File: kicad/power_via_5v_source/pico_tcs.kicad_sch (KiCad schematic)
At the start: 11 parts, among them J1 TCS/Power, J2 Conn_01x20_Male, J3 Conn_01x20_Male, J4 Keypad, J5 Display, U2 ULN2003

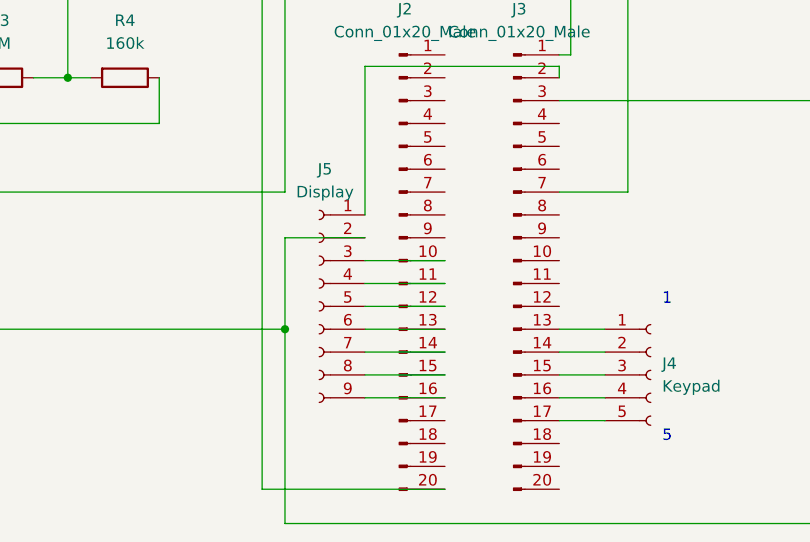
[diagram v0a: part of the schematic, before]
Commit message: fixed bug in connection between display and pico
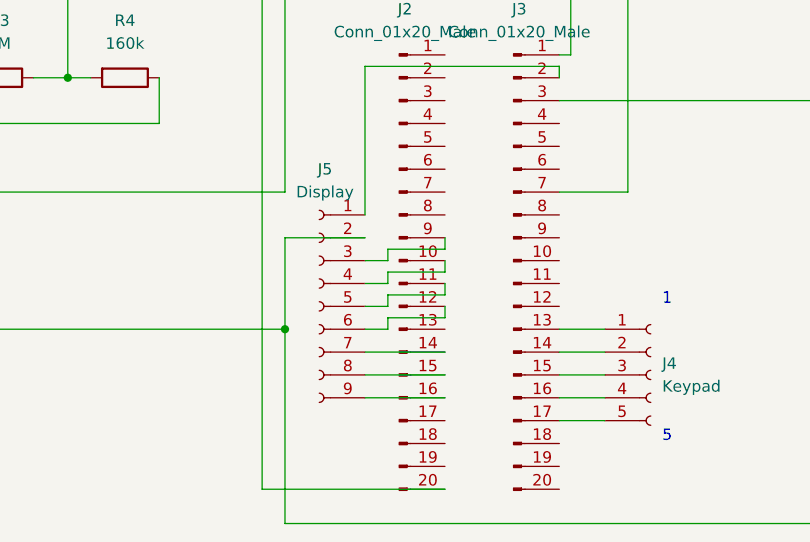
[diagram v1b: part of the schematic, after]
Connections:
- net at J5.3 (Pin_3): now also J2.9 (Pin_9); no longer J2.10 (Pin_10)
- net at J5.4 (Pin_4): now also J2.10 (Pin_10); no longer J2.11 (Pin_11)
- net at J5.5 (Pin_5): now also J2.11 (Pin_11); no longer J2.12 (Pin_12)
- net at J5.6 (Pin_6): now also J2.12 (Pin_12); no longer J2.13 (Pin_13)
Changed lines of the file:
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@@
+    (stroke (width 0) (type default) (color 0 0 0 0))
+  )
+  (wire (pts (xy 121.92 62.23) (xy 121.92 60.96))
     (stroke (width 0) (type default) (color 0 0 0 0))
   )
@@
     (stroke (width 0) (type default) (color 0 0 0 0))
   )
+  (wire (pts (xy 128.27 60.96) (xy 128.27 59.69))
+    (stroke (width 0) (type default) (color 0 0 0 0))
+  )
   (wire (pts (xy 71.12 69.85) (xy 110.49 69.85))
     (stroke (width 0) (type default) (color 0 0 0 0))
   )
-  (wire (pts (xy 119.38 69.85) (xy 128.27 69.85))
+  (wire (pts (xy 96.52 46.99) (xy 66.04 46.99))
     (stroke (width 0) (type default) (color 0 0 0 0))
   )
-  (wire (pts (xy 96.52 46.99) (xy 66.04 46.99))
+  (wire (pts (xy 128.27 64.77) (xy 128.27 66.04))
     (stroke (width 0) (type default) (color 0 0 0 0))
   )
@@
     (stroke (width 0) (type default) (color 0 0 0 0))
   )
+  (wire (pts (xy 119.38 62.23) (xy 121.92 62.23))
+    (stroke (width 0) (type default) (color 0 0 0 0))
+  )
   (wire (pts (xy 64.77 33.02) (xy 72.39 33.02))
     (stroke (width 0) (type default) (color 0 0 0 0))
   )
   (wire (pts (xy 71.12 54.61) (xy 71.12 60.96))
-    (stroke (width 0) (type default) (color 0 0 0 0))
-  )
-  (wire (pts (xy 119.38 62.23) (xy 128.27 62.23))
     (stroke (width 0) (type default) (color 0 0 0 0))
   )
@@
     (stroke (width 0) (type default) (color 0 0 0 0))
   )
+  (wire (pts (xy 119.38 64.77) (xy 121.92 64.77))
+    (stroke (width 0) (type default) (color 0 0 0 0))
+  )
+  (wire (pts (xy 121.92 63.5) (xy 128.27 63.5))
+    (stroke (width 0) (type default) (color 0 0 0 0))
+  )
   (wire (pts (xy 54.61 25.4) (xy 64.77 25.4))
+    (stroke (width 0) (type default) (color 0 0 0 0))
+  )
+  (wire (pts (xy 128.27 68.58) (xy 128.27 67.31))
     (stroke (width 0) (type default) (color 0 0 0 0))
   )
@@
     (stroke (width 0) (type default) (color 0 0 0 0))
   )
+  (wire (pts (xy 121.92 67.31) (xy 121.92 66.04))
+    (stroke (width 0) (type default) (color 0 0 0 0))
+  )
   (wire (pts (xy 38.1 62.23) (xy 64.77 62.23))
+    (stroke (width 0) (type default) (color 0 0 0 0))
+  )
+  (wire (pts (xy 121.92 64.77) (xy 121.92 63.5))
+    (stroke (width 0) (type default) (color 0 0 0 0))
+  )
+  (wire (pts (xy 121.92 66.04) (xy 128.27 66.04))
     (stroke (width 0) (type default) (color 0 0 0 0))
   )
@@
     (stroke (width 0) (type default) (color 0 0 0 0))
   )
+  (wire (pts (xy 119.38 67.31) (xy 121.92 67.31))
+    (stroke (width 0) (type default) (color 0 0 0 0))
+  )
   (wire (pts (xy 119.38 40.64) (xy 140.97 40.64))
     (stroke (width 0) (type default) (color 0 0 0 0))
   )
   (wire (pts (xy 119.38 77.47) (xy 128.27 77.47))
+    (stroke (width 0) (type default) (color 0 0 0 0))
+  )
+  (wire (pts (xy 119.38 69.85) (xy 121.92 69.85))
     (stroke (width 0) (type default) (color 0 0 0 0))
   )
@@
     (stroke (width 0) (type default) (color 0 0 0 0))
   )
+  (wire (pts (xy 121.92 69.85) (xy 121.92 68.58))
+    (stroke (width 0) (type default) (color 0 0 0 0))
+  )
   (wire (pts (xy 119.38 74.93) (xy 128.27 74.93))
     (stroke (width 0) (type default) (color 0 0 0 0))
@@
     (stroke (width 0) (type default) (color 0 0 0 0))
   )
-  (wire (pts (xy 168.91 44.45) (xy 140.97 44.45))
+  (wire (pts (xy 128.27 62.23) (xy 128.27 63.5))
     (stroke (width 0) (type default) (color 0 0 0 0))
   )
-  (wire (pts (xy 119.38 64.77) (xy 128.27 64.77))
+  (wire (pts (xy 168.91 44.45) (xy 140.97 44.45))
     (stroke (width 0) (type default) (color 0 0 0 0))
   )
@@
   )
   (wire (pts (xy 64.77 67.31) (xy 67.31 67.31))
-    (stroke (width 0) (type default) (color 0 0 0 0))
-  )
-  (wire (pts (xy 119.38 67.31) (xy 128.27 67.31))
     (stroke (width 0) (type default) (color 0 0 0 0))
   )
@@
     (stroke (width 0) (type default) (color 0 0 0 0))
   )
+  (wire (pts (xy 121.92 68.58) (xy 128.27 68.58))
+    (stroke (width 0) (type default) (color 0 0 0 0))
+  )
   (wire (pts (xy 16.51 24.13) (xy 16.51 20.32))
     (stroke (width 0) (type default) (color 0 0 0 0))
@@
     (stroke (width 0) (type default) (color 0 0 0 0))
   )
+  (wire (pts (xy 121.92 60.96) (xy 128.27 60.96))
+    (stroke (width 0) (type default) (color 0 0 0 0))
+  )
